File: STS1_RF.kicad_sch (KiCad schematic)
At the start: 82 parts, among them J1 UHF, Q1 SQ2318, Q3 SQ2318, Q4 SQ2318, U10 TQP3M9036, U11 NL17SV04XV5T2G, U16 F2972, U2 LP2985-1.8, U30 TMP36xS, U4 74LVC2G74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

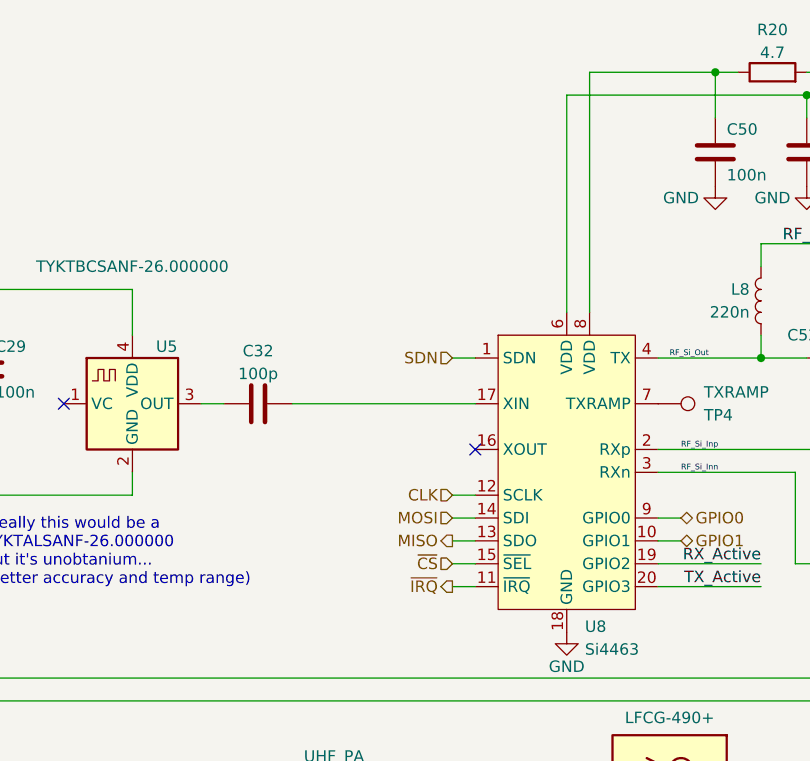
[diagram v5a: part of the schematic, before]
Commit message: Fix power domain crossing issue between RF and STM units
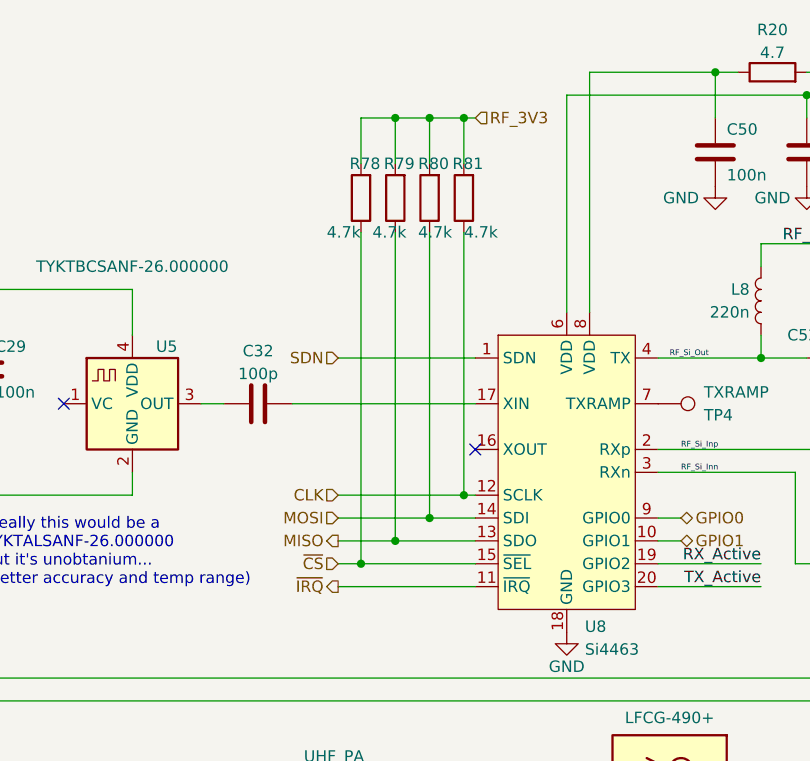
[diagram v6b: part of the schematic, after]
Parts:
- added R78, R79, R80, R81: 4.7k, Resistor_SMD:R_0603_1608Metric, symbol Device:R
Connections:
- net CLK: now also R81.1
- net MISO: now also R79.1
- net MOSI: now also R80.1
- net VCC: now also R78.2, R79.2, R80.2, R81.2
- net ~{CS}: now also R78.1

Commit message: Update the manufacturer part number for some of components to be compatible with avaiable parts in the JLC parts database
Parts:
- C1, C27, C29, C50, C64, C7, C8: JLCPCB Part # C1711 -> C141125; Manufacturer_Part_Number CL21B104KBCNNNC -> C0805C104K1RACAUTO
- C2, C28: JLCPCB Part # C722528 -> C599948; Manufacturer_Part_Number CL21A475KAQNNNG -> C0805C475K4RACAUTO
- C26, C55: JLCPCB Part # C7224472 -> C561833
- C48, C65: JLCPCB Part # (none) -> C3874210; Manufacturer_Part_Number C0402C105K8PAC7411 -> C0805C105K5RACAUTO
- C59: JLCPCB Part # (none) -> C3008877; Manufacturer_Part_Number CL21A476MQYNNWE -> T58W9476M6R3C0200
- C69: JLCPCB Part # (none) -> C326803; Manufacturer_Part_Number 500R07S150KV4T -> CC0402FRNPO9BN150
- C94: JLCPCB Part # C1591 -> C129621; Manufacturer_Part_Number CL10B104KB8NNNC -> C0603C104K5RACAUTO
- Q3, Q4: Manufacturer_Part_Number SQ2318AES-T1_BE3 -> SQ2318AES-T1_BE3
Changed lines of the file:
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@@
       (effects (font (size 1.27 1.27)) hide)
     )
-    (property "JLCPCB Part #" "C722528" (id 4) (at 187.96 27.94 0)
-      (effects (font (size 1.27 1.27)) hide)
-    )
-    (property "Manufacturer_Part_Number" "CL21A475KAQNNNG " (id 5) (at 187.96 27.94 0)
+    (property "JLCPCB Part #" "C599948" (id 4) (at 187.96 27.94 0)
+      (effects (font (size 1.27 1.27)) hide)
+    )
+    (property "Manufacturer_Part_Number" "C0805C475K4RACAUTO" (id 5) (at 187.96 27.94 0)
       (effects (font (size 1.27 1.27)) hide)
     )
@@
       (effects (font (size 1.27 1.27)) hide)
     )
-    (property "JLCPCB Part #" "C1711" (id 4) (at 180.34 27.94 0)
-      (effects (font (size 1.27 1.27)) hide)
-    )
-    (property "Manufacturer_Part_Number" "CL21B104KBCNNNC " (id 5) (at 180.34 27.94 0)
+    (property "JLCPCB Part #" "C141125" (id 4) (at 180.34 27.94 0)
+      (effects (font (size 1.27 1.27)) hide)
+    )
+    (property "Manufacturer_Part_Number" "C0805C104K1RACAUTO" (id 5) (at 180.34 27.94 0)
       (effects (font (size 1.27 1.27)) hide)
     )
@@
       (effects (font (size 1.27 1.27)) hide)
     )
-    (property "Manufacturer_Part_Number" "500R07S150KV4T " (id 4) (at 185.42 57.15 0)
+    (property "Manufacturer_Part_Number" "CC0402FRNPO9BN150" (id 4) (at 185.42 57.15 0)
+      (effects (font (size 1.27 1.27)) hide)
+    )
+    (property "JLCPCB Part #" "C326803" (id 5) (at 185.42 57.15 0)
       (effects (font (size 1.27 1.27)) hide)
     )
@@
       (effects (font (size 1.27 1.27)) hide)
     )
-    (property "JLCPCB Part #" "C1711" (id 4) (at 147.32 27.94 0)
-      (effects (font (size 1.27 1.27)) hide)
-    )
-    (property "Manufacturer_Part_Number" "CL21B104KBCNNNC " (id 5) (at 147.32 27.94 0)
+    (property "JLCPCB Part #" "C141125" (id 4) (at 147.32 27.94 0)
+      (effects (font (size 1.27 1.27)) hide)
+    )
+    (property "Manufacturer_Part_Number" "C0805C104K1RACAUTO" (id 5) (at 147.32 27.94 0)
       (effects (font (size 1.27 1.27)) hide)
     )
@@
       (effects (font (size 1.27 1.27)) hide)
     )
-    (property "Manufacturer_Part_Number" "C0402C105K8PAC7411 " (id 7) (at 129.54 149.86 0)
+    (property "Manufacturer_Part_Number" "C0805C105K5RACAUTO" (id 7) (at 129.54 149.86 0)
+      (effects (font (size 1.27 1.27)) hide)
+    )
+    (property "JLCPCB Part #" "C3874210" (id 8) (at 129.54 149.86 0)
       (effects (font (size 1.27 1.27)) hide)
     )
@@
       (effects (font (size 1.27 1.27)) hide)
     )
-    (property "JLCPCB Part #" "C1711" (id 4) (at 256.54 107.95 0)
-      (effects (font (size 1.27 1.27)) hide)
-    )
-    (property "Manufacturer_Part_Number" "CL21B104KBCNNNC " (id 5) (at 256.54 107.95 0)
+    (property "JLCPCB Part #" "C141125" (id 4) (at 256.54 107.95 0)
+      (effects (font (size 1.27 1.27)) hide)
+    )
+    (property "Manufacturer_Part_Number" "C0805C104K1RACAUTO" (id 5) (at 256.54 107.95 0)
       (effects (font (size 1.27 1.27)) hide)
     )
@@
       (effects (font (size 1.27 1.27)) hide)
     )
-    (property "Manufacturer_Part_Number" "SQ2318AES-T1_BE3 " (id 4) (at 68.58 162.56 0)
+    (property "Manufacturer_Part_Number" "SQ2318AES-T1_BE3" (id 4) (at 68.58 162.56 0)
       (effects (font (size 1.27 1.27)) hide)
     )
@@
       (effects (font (size 1.27 1.27)) hide)
     )
-    (property "JLCPCB Part #" "C7224472" (id 4) (at 172.72 27.94 0)
+    (property "JLCPCB Part #" "C561833" (id 4) (at 172.72 27.94 0)
       (effects (font (size 1.27 1.27)) hide)
     )
@@
       (effects (font (size 1.27 1.27)) hide)
     )
-    (property "JLCPCB Part #" "C1711" (id 4) (at 66.04 52.07 0)
-      (effects (font (size 1.27 1.27)) hide)
-    )
-    (property "Manufacturer_Part_Number" "CL21B104KBCNNNC " (id 5) (at 66.04 52.07 0)
+    (property "JLCPCB Part #" "C141125" (id 4) (at 66.04 52.07 0)
+      (effects (font (size 1.27 1.27)) hide)
+    )
+    (property "Manufacturer_Part_Number" "C0805C104K1RACAUTO" (id 5) (at 66.04 52.07 0)
       (effects (font (size 1.27 1.27)) hide)
     )
@@
       (effects (font (size 1.27 1.27)) hide)
     )
-    (property "Manufacturer_Part_Number" "CL21A476MQYNNWE " (id 4) (at 195.58 27.94 0)
+    (property "Manufacturer_Part_Number" "T58W9476M6R3C0200" (id 4) (at 195.58 27.94 0)
+      (effects (font (size 1.27 1.27)) hide)
+    )
+    (property "JLCPCB Part #" "C3008877" (id 5) (at 195.58 27.94 0)
       (effects (font (size 1.27 1.27)) hide)
     )
@@
       (effects (font (size 1.27 1.27)) hide)
     )
-    (property "JLCPCB Part #" "C1711" (id 4) (at 27.94 127 0)
-      (effects (font (size 1.27 1.27)) hide)
-    )
-    (property "Manufacturer_Part_Number" "CL21B104KBCNNNC " (id 5) (at 27.94 127 0)
+    (property "JLCPCB Part #" "C141125" (id 4) (at 27.94 127 0)
+      (effects (font (size 1.27 1.27)) hide)
+    )
+    (property "Manufacturer_Part_Number" "C0805C104K1RACAUTO" (id 5) (at 27.94 127 0)
       (effects (font (size 1.27 1.27)) hide)
     )
@@
       (effects (font (size 1.27 1.27)) hide)
     )
-    (property "JLCPCB Part #" "C1591" (id 4) (at 261.493 52.324 0)
-      (effects (font (size 1.27 1.27)) hide)
-    )
-    (property "Manufacturer_Part_Number" "CL10B104KB8NNNC " (id 5) (at 261.493 52.324 0)
+    (property "JLCPCB Part #" "C129621" (id 4) (at 261.493 52.324 0)
+      (effects (font (size 1.27 1.27)) hide)
+    )
+    (property "Manufacturer_Part_Number" "C0603C104K5RACAUTO" (id 5) (at 261.493 52.324 0)
       (effects (font (size 1.27 1.27)) hide)
     )
@@
       (effects (font (size 1.27 1.27)) hide)
     )
-    (property "JLCPCB Part #" "C722528" (id 4) (at 57.15 52.07 0)
-      (effects (font (size 1.27 1.27)) hide)
-    )
-    (property "Manufacturer_Part_Number" "CL21A475KAQNNNG " (id 5) (at 57.15 52.07 0)
+    (property "JLCPCB Part #" "C599948" (id 4) (at 57.15 52.07 0)
+      (effects (font (size 1.27 1.27)) hide)
+    )
+    (property "Manufacturer_Part_Number" "C0805C475K4RACAUTO" (id 5) (at 57.15 52.07 0)
       (effects (font (size 1.27 1.27)) hide)
     )
@@
       (effects (font (size 1.27 1.27)) hide)
     )
-    (property "JLCPCB Part #" "C1711" (id 4) (at 165.1 160.02 0)
-      (effects (font (size 1.27 1.27)) hide)
-    )
-    (property "Manufacturer_Part_Number" "CL21B104KBCNNNC " (id 5) (at 165.1 160.02 0)
+    (property "JLCPCB Part #" "C141125" (id 4) (at 165.1 160.02 0)
+      (effects (font (size 1.27 1.27)) hide)
+    )
+    (property "Manufacturer_Part_Number" "C0805C104K1RACAUTO" (id 5) (at 165.1 160.02 0)
       (effects (font (size 1.27 1.27)) hide)
     )
@@
       (effects (font (size 1.27 1.27)) hide)
     )
-    (property "Manufacturer_Part_Number" "C0402C105K8PAC7411 " (id 4) (at 264.16 107.95 0)
+    (property "Manufacturer_Part_Number" "C0805C105K5RACAUTO" (id 4) (at 264.16 107.95 0)
+      (effects (font (size 1.27 1.27)) hide)
+    )
+    (property "JLCPCB Part #" "C3874210" (id 5) (at 264.16 107.95 0)
       (effects (font (size 1.27 1.27)) hide)
     )
@@
       (effects (font (size 1.27 1.27)) hide)
     )
-    (property "JLCPCB Part #" "C7224472" (id 4) (at 48.26 52.07 0)
+    (property "JLCPCB Part #" "C561833" (id 4) (at 48.26 52.07 0)
       (effects (font (size 1.27 1.27)) hide)
     )
@@
       (effects (font (size 1.27 1.27)) hide)
     )
-    (property "JLCPCB Part #" "C1711" (id 4) (at 22.86 52.07 0)
-      (effects (font (size 1.27 1.27)) hide)
-    )
-    (property "Manufacturer_Part_Number" "CL21B104KBCNNNC " (id 5) (at 22.86 52.07 0)
+    (property "JLCPCB Part #" "C141125" (id 4) (at 22.86 52.07 0)
+      (effects (font (size 1.27 1.27)) hide)
+    )
+    (property "Manufacturer_Part_Number" "C0805C104K1RACAUTO" (id 5) (at 22.86 52.07 0)
       (effects (font (size 1.27 1.27)) hide)
     )
@@
       (effects (font (size 1.27 1.27)) hide)
     )
-    (property "Manufacturer_Part_Number" "SQ2318AES-T1_BE3 " (id 4) (at 91.44 154.94 0)
-      (effects (font (size 1.27 1.27)) hide)
-    )
+    (property "Manufacturer_Part_Number" "SQ2318AES-T1_BE3" (id 4) (at 91.44 154.94 0)
+      (effects (font (size 1.27 1.27)) hide)
+    )

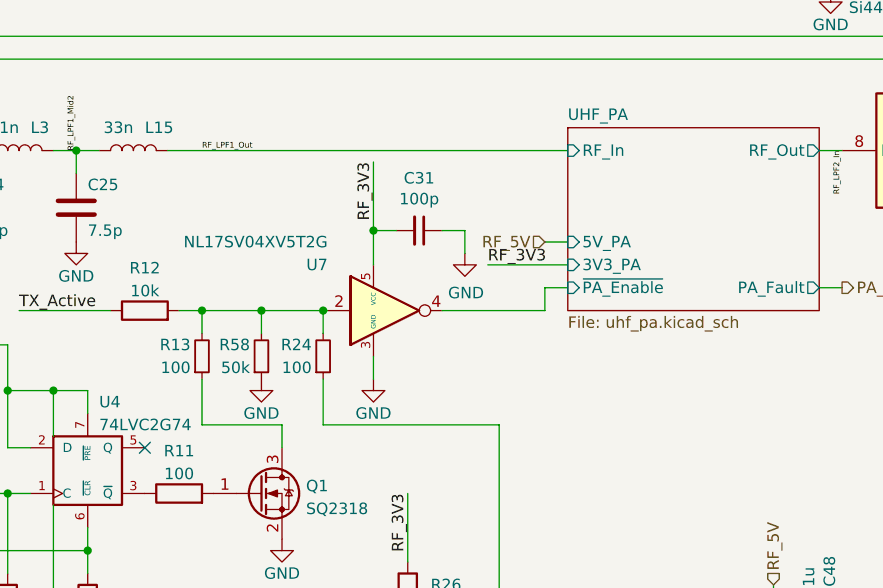
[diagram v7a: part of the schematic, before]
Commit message: Replace the U12 from FPF2702 to TPS22950-Q1: R30 is pulling down, R31: 110K -> 470 Ohm, U7 is removed, since ON is active high now
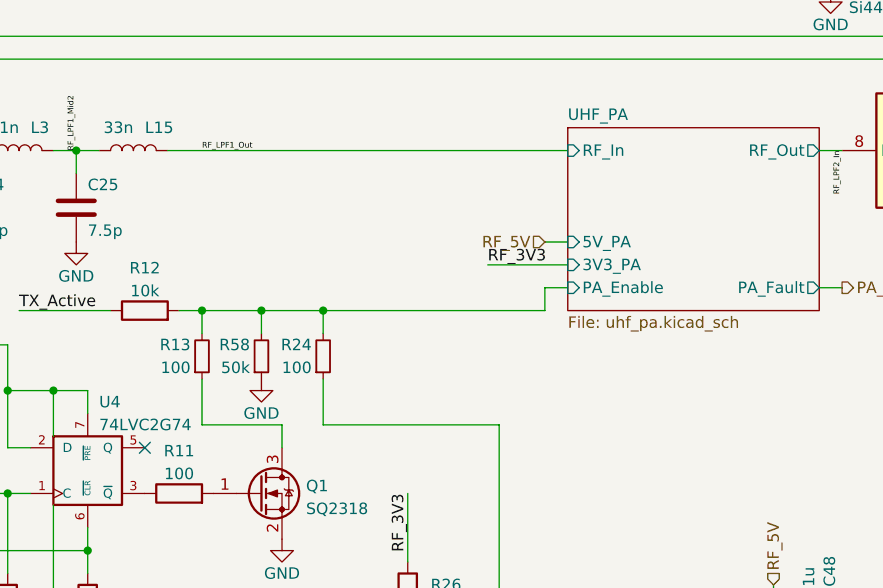
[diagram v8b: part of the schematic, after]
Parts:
- removed C31: 100p, Capacitor_SMD:C_0402_1005Metric, symbol Device:C_Small
- removed U7: NL17SV04XV5T2G, Package_TO_SOT_SMD:SOT-553, symbol 74xGxx:74LVC1GU04DRL
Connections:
- net UHF_PA/PA_Enable: now reaches R12.2, R13.2, R24.2, R58.2
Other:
- sheet UHF_PA ports: added PA_Enable; removed ~{PA_Enable}
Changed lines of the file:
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@@
   (junction (at 134.62 154.94) (diameter 0) (color 0 0 0 0)
   )
-  (junction (at 80.01 107.95) (diameter 0) (color 0 0 0 0)
-  )
   (junction (at 57.15 66.04) (diameter 0) (color 0 0 0 0)
   )
@@
     (stroke (width 0) (type default) (color 0 0 0 0))
   )
-  (wire (pts (xy 90.17 107.95) (xy 90.17 110.49))
-    (stroke (width 0) (type default) (color 0 0 0 0))
-  )
   (wire (pts (xy 115.57 36.83) (xy 115.57 68.58))
     (stroke (width 0) (type default) (color 0 0 0 0))
@@
     (stroke (width 0) (type default) (color 0 0 0 0))
   )
-  (wire (pts (xy 80.01 100.33) (xy 80.01 107.95))
-    (stroke (width 0) (type default) (color 0 0 0 0))
-  )
   (wire (pts (xy 69.85 129.54) (xy 69.85 132.08))
     (stroke (width 0) (type default) (color 0 0 0 0))
@@
     (stroke (width 0) (type default) (color 0 0 0 0))
   )
-  (wire (pts (xy 74.422 116.84) (xy 74.93 116.84))
-    (stroke (width 0) (type default) (color 0 0 0 0))
-  )
-  (wire (pts (xy 87.63 116.84) (xy 99.06 116.84))
+  (wire (pts (xy 74.422 116.84) (xy 99.06 116.84))
     (stroke (width 0) (type default) (color 0 0 0 0))
   )
@@
     (stroke (width 0) (type default) (color 0 0 0 0))
   )
-  (wire (pts (xy 80.01 121.92) (xy 80.01 124.46))
-    (stroke (width 0) (type default) (color 0 0 0 0))
-  )
   (wire (pts (xy 195.58 21.59) (xy 218.44 21.59))
     (stroke (width 0) (type default) (color 0 0 0 0))
@@
     (stroke (width 0) (type default) (color 0 0 0 0))
   )
-  (wire (pts (xy 80.01 111.76) (xy 80.01 107.95))
-    (stroke (width 0) (type default) (color 0 0 0 0))
-  )
   (wire (pts (xy 105.41 71.12) (xy 111.76 71.12))
     (stroke (width 0) (type default) (color 0 0 0 0))
@@
     (stroke (width 0) (type default) (color 0 0 0 0))
   )
-  (wire (pts (xy 87.63 107.95) (xy 90.17 107.95))
-    (stroke (width 0) (type default) (color 0 0 0 0))
-  )
   (wire (pts (xy 185.42 50.8) (xy 185.42 53.34))
     (stroke (width 0) (type default) (color 0 0 0 0))
@@
     (stroke (width 0) (type default) (color 0 0 0 0))
   )
-  (wire (pts (xy 82.55 107.95) (xy 80.01 107.95))
-    (stroke (width 0) (type default) (color 0 0 0 0))
-  )
   (wire (pts (xy 41.91 132.08) (xy 39.37 132.08))
     (stroke (width 0) (type default) (color 0 0 0 0))
@@
     (effects (font (size 0.635 0.635)) (justify left bottom))
   )
-  (label "RF_3V3" (at 80.01 100.33 270)
-    (effects (font (size 1.27 1.27)) (justify right bottom))
-  )
   (label "RF_Sw" (at 250.19 130.81 0) (fields_autoplaced)
     (effects (font (size 0.635 0.635)) (justify left bottom))
@@
     (pin "2")
   )
-  (symbol (lib_id "74xGxx:74LVC1GU04DRL") (at 80.01 116.84 0) (unit 1)
-    (in_bom yes) (on_board yes)
-    (property "Reference" "U7" (id 0) (at 74.93 111.76 0)
-      (effects (font (size 1.27 1.27)) (justify right))
-    )
-    (property "Value" "NL17SV04XV5T2G" (id 1) (at 74.93 109.22 0)
-      (effects (font (size 1.27 1.27)) (justify right))
-    )
-    (property "Footprint" "Package_TO_SOT_SMD:SOT-553" (id 2) (at 80.01 123.19 0)
-      (effects (font (size 1.27 1.27)) hide)
-    )
-    (property "Datasheet" "http://www.ti.com/lit/ds/symlink/sn74lvc1gu04.pdf" (id 3) (at 78.105 116.84 0)
-      (effects (font (size 1.27 1.27)) hide)
-    )
-    (property "PartNumber" "NL17SV04XV5T2G" (id 4) (at 80.01 116.84 0)
-      (effects (font (size 1.27 1.27)) hide)
-    )
-    (property "Mnf." "Nexperia" (id 5) (at 80.01 116.84 0)
-      (effects (font (size 1.27 1.27)) hide)
-    )
-    (property "Manufacturer_Part_Number" "NL17SV04XV5T2G " (id 6) (at 80.01 116.84 0)
-      (effects (font (size 1.27 1.27)) hide)
-    )
-    (property "JLCPCB Part #" "C185507" (id 7) (at 80.01 116.84 0)
-      (effects (font (size 1.27 1.27)) hide)
-    )
-    (pin "1")
-    (pin "2")
-    (pin "3")
-    (pin "4")
-    (pin "5")
-  )
   (symbol (lib_id "power:GND") (at 137.16 186.69 0) (unit 1)
     (in_bom yes) (on_board yes)
@@
     (pin "1")
   )
-  (symbol (lib_id "Device:C_Small") (at 85.09 107.95 270) (unit 1)
-    (in_bom yes) (on_board yes)
-    (property "Reference" "C31" (id 0) (at 85.09 102.1334 90))
-    (property "Value" "100p" (id 1) (at 85.09 104.4448 90))
-    (property "Footprint" "Capacitor_SMD:C_0402_1005Metric" (id 2) (at 85.09 107.95 0)
-      (effects (font (size 1.27 1.27)) hide)
-    )
-    (property "Datasheet" "~" (id 3) (at 85.09 107.95 0)
-      (effects (font (size 1.27 1.27)) hide)
-    )
-    (property "Description" "Capacitor, 0402, 5%, 50V, NPO/COG" (id 4) (at 85.09 107.95 0)
-      (effects (font (size 1.27 1.27)) hide)
-    )
-    (property "Mnf." "KEMET" (id 5) (at 85.09 107.95 0)
-      (effects (font (size 1.27 1.27)) hide)
-    )
-    (property "PartNumber" "CBR04C101J3GAC" (id 6) (at 85.09 107.95 0)
-      (effects (font (size 1.27 1.27)) hide)
-    )
-    (property "JLCPCB Part #" "C386123" (id 7) (at 85.09 107.95 0)
-      (effects (font (size 1.27 1.27)) hide)
-    )
-    (property "Manufacturer_Part_Number" "UMK105CG101JV-F" (id 8) (at 85.09 107.95 0)
-      (effects (font (size 1.27 1.27)) hide)
-    )
-    (pin "1")
-    (pin "2")
-  )
   (symbol (lib_id "Device:L") (at 152.4 44.45 180) (unit 1)
     (in_bom yes) (on_board yes)
@@
     (pin "1")
   )
-  (symbol (lib_id "power:GND") (at 80.01 124.46 0) (unit 1)
-    (in_bom yes) (on_board yes)
-    (property "Reference" "#PWR0178" (id 0) (at 80.01 130.81 0)
-      (effects (font (size 1.27 1.27)) hide)
-    )
-    (property "Value" "GND" (id 1) (at 80.01 128.27 0))
-    (property "Footprint" "" (id 2) (at 80.01 124.46 0)
-      (effects (font (size 1.27 1.27)) hide)
-    )
-    (property "Datasheet" "" (id 3) (at 80.01 124.46 0)
-      (effects (font (size 1.27 1.27)) hide)
-    )
-    (pin "1")
-  )
   (symbol (lib_id "Device:C") (at 260.35 130.81 90) (unit 1)
     (in_bom yes) (on_board yes)
@@
     (pin "1")
   )
-  (symbol (lib_id "power:GND") (at 90.17 110.49 0) (unit 1)
-    (in_bom yes) (on_board yes)
-    (property "Reference" "#PWR0175" (id 0) (at 90.17 116.84 0)
-      (effects (font (size 1.27 1.27)) hide)
-    )
-    (property "Value" "GND" (id 1) (at 90.297 114.8842 0))
-    (property "Footprint" "" (id 2) (at 90.17 110.49 0)
-      (effects (font (size 1.27 1.27)) hide)
-    )
-    (property "Datasheet" "" (id 3) (at 90.17 110.49 0)
-      (effects (font (size 1.27 1.27)) hide)
-    )
-    (pin "1")
-  )
   (symbol (lib_id "power:GND") (at 138.43 156.21 0) (unit 1)
     (in_bom yes) (on_board yes)
@@
       (effects (font (size 1.27 1.27)) (justify left))
     )
-    (pin "~{PA_Enable}" input (at 101.6 114.3 180)
+    (pin "PA_Enable" input (at 101.6 114.3 180)
       (effects (font (size 1.27 1.27)) (justify left))
     )
